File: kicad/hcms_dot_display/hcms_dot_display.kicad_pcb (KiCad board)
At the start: 2 copper layers, 35.6 x 42.1 mm, 36 parts, among them J1 Conn_01x13, J2 USB_C_Receptacle_USB2.0, J3 Conn_01x13, J4 Conn_01x10_Female, J5 Conn_01x10_Male, Q1 Q_PMOS_DSG, Q2 Q_PMOS_DSG, Q3 Q_PMOS_DSG, Q4 Q_PMOS_DSG, Q5 Q_PMOS_DSG, U1 ATtiny824-SSF, U2 FT231XS

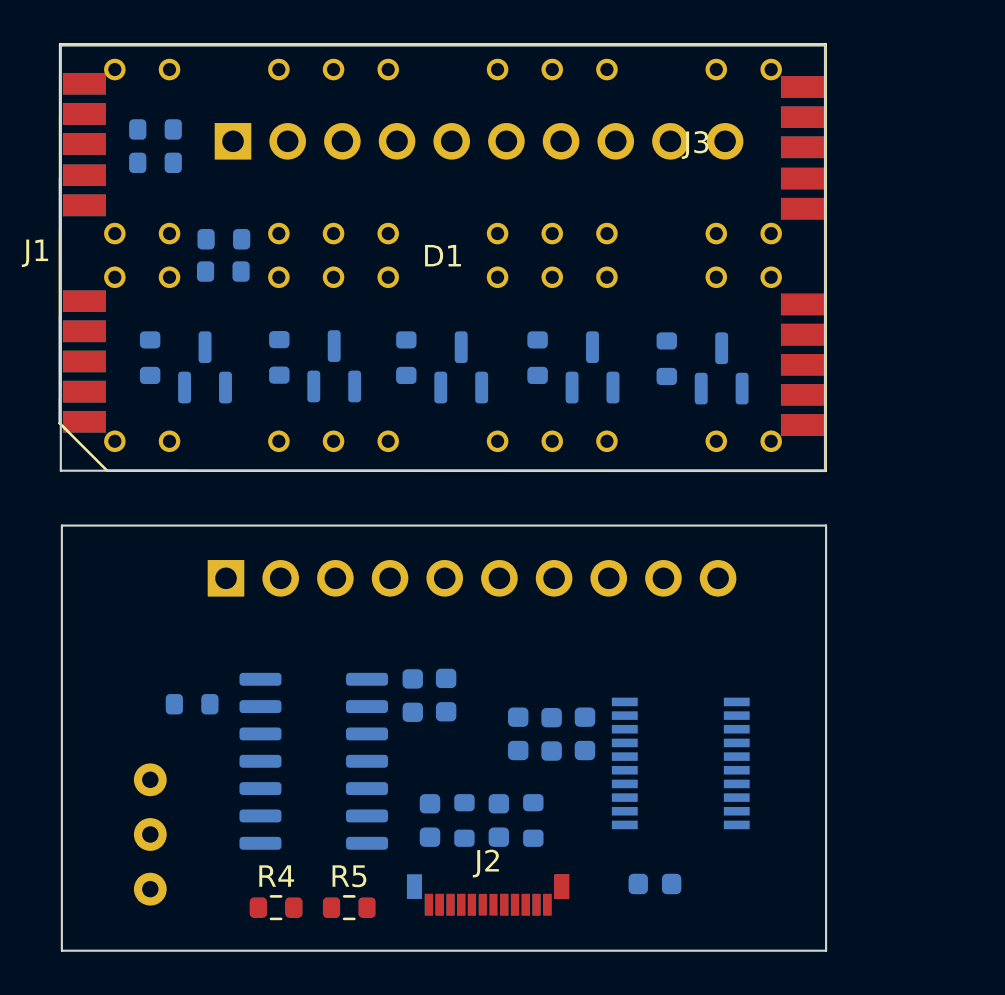
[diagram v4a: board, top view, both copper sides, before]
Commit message: fixed pot footprint, updated layout from schematics, changed board to board conn sch sym from 13 pin to 11 pin, reorgd sch sym to reflect stacked board design, added decoupling caps to top board
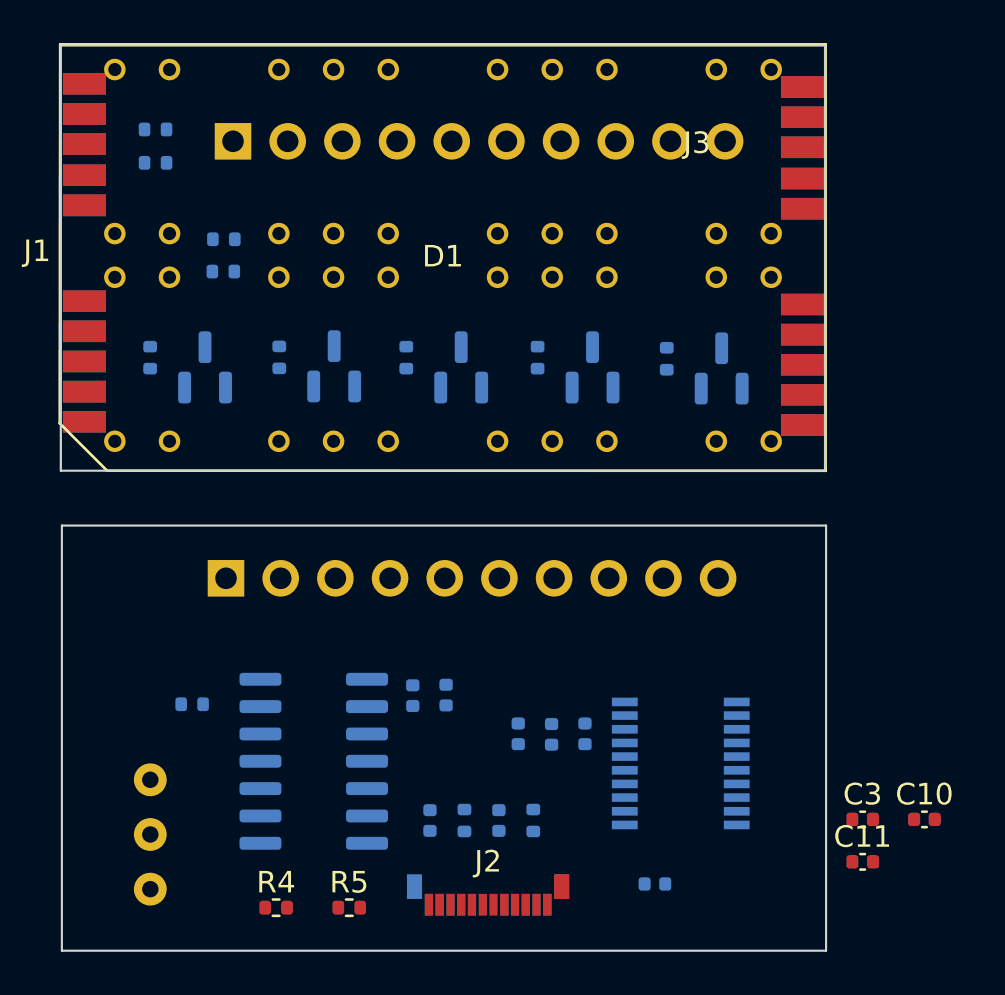
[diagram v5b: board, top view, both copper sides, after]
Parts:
- added C10: 10nF, Capacitor_SMD:C_0402_1005Metric, F.Cu at (174.9, 132.2)
- added C11: 10nF, Capacitor_SMD:C_0402_1005Metric, F.Cu at (172.0, 134.2)
- added C3: 100nF, Capacitor_SMD:C_0402_1005Metric, F.Cu at (172.0, 132.2)
- C1, C2, C4, C5, C6, C7, C8, C9: footprint Capacitor_SMD:C_0603_1608Metric -> Capacitor_SMD:C_0402_1005Metric
- R1, R10, R11, R12, R13, R14, R15, R2, R4, R5, R6, R7, R8, R9: footprint Resistor_SMD:R_0603_1608Metric -> Resistor_SMD:R_0402_1005Metric
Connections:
- J1 pad 10: /B_DATA -> /DAISY_B_DATA
- J1 pad 9: /A_DATA -> /DAISY_A_DATA
- J4 pad 1: /nBLNK -> +5V
- J4 pad 2: /MCU_DATA -> /MCU_COL_1
- J4 pad 3: /CLK -> /MCU_COL_2
- J4 pad 4: /MCU_COL_5 -> /MCU_COL_3
- J4 pad 6: /MCU_COL_3 -> /MCU_COL_5
- J4 pad 7: /MCU_COL_2 -> /nBLNK
- J4 pad 8: /MCU_COL_1 -> /CLK
- J4 pad 9: +5V -> /MCU_DATA
- J5 pad 1: /nBLNK -> +5V
- J5 pad 2: /MCU_DATA -> /MCU_COL_1
- J5 pad 3: /CLK -> /MCU_COL_2
- J5 pad 4: /MCU_COL_5 -> /MCU_COL_3
- J5 pad 6: /MCU_COL_3 -> /MCU_COL_5
- J5 pad 7: /MCU_COL_2 -> /nBLNK
- J5 pad 8: /MCU_COL_1 -> /CLK
- J5 pad 9: +5V -> /MCU_DATA

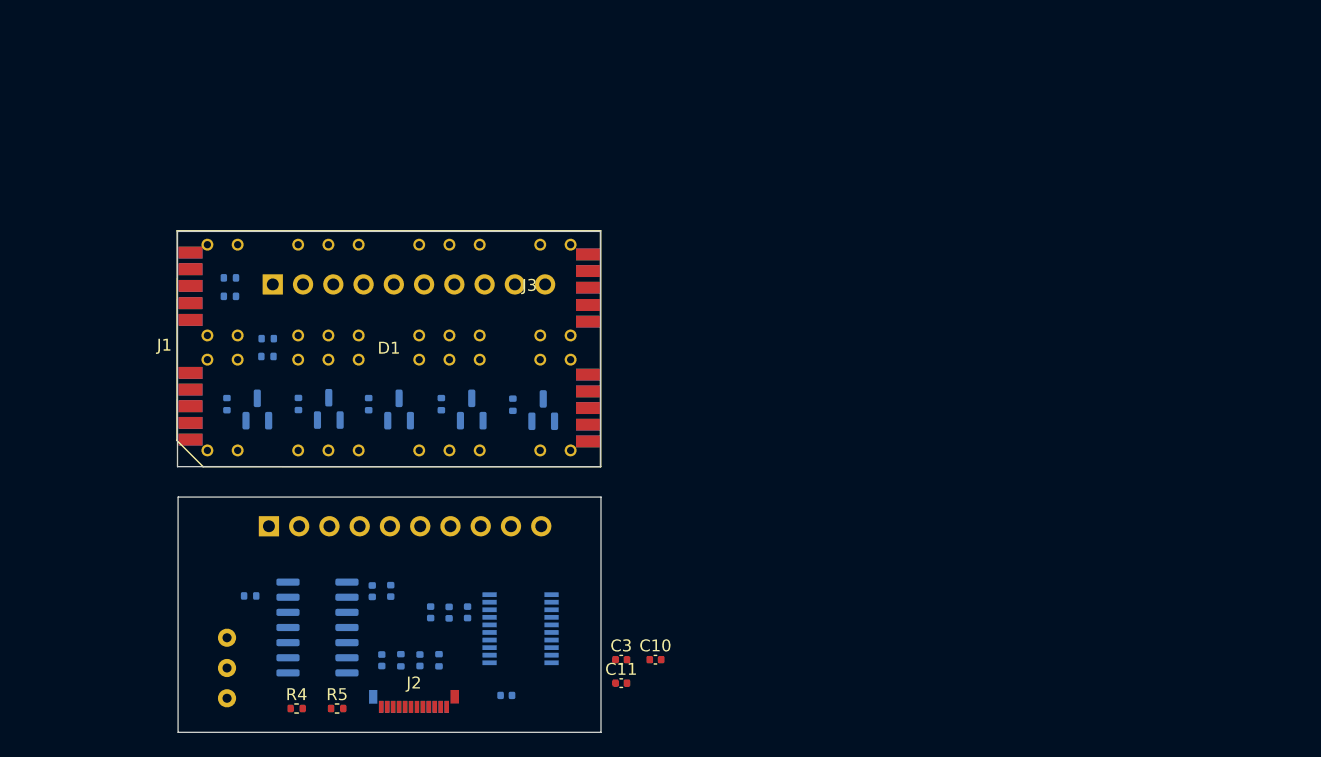
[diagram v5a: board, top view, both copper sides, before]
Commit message: fixed some footprints and edited placement
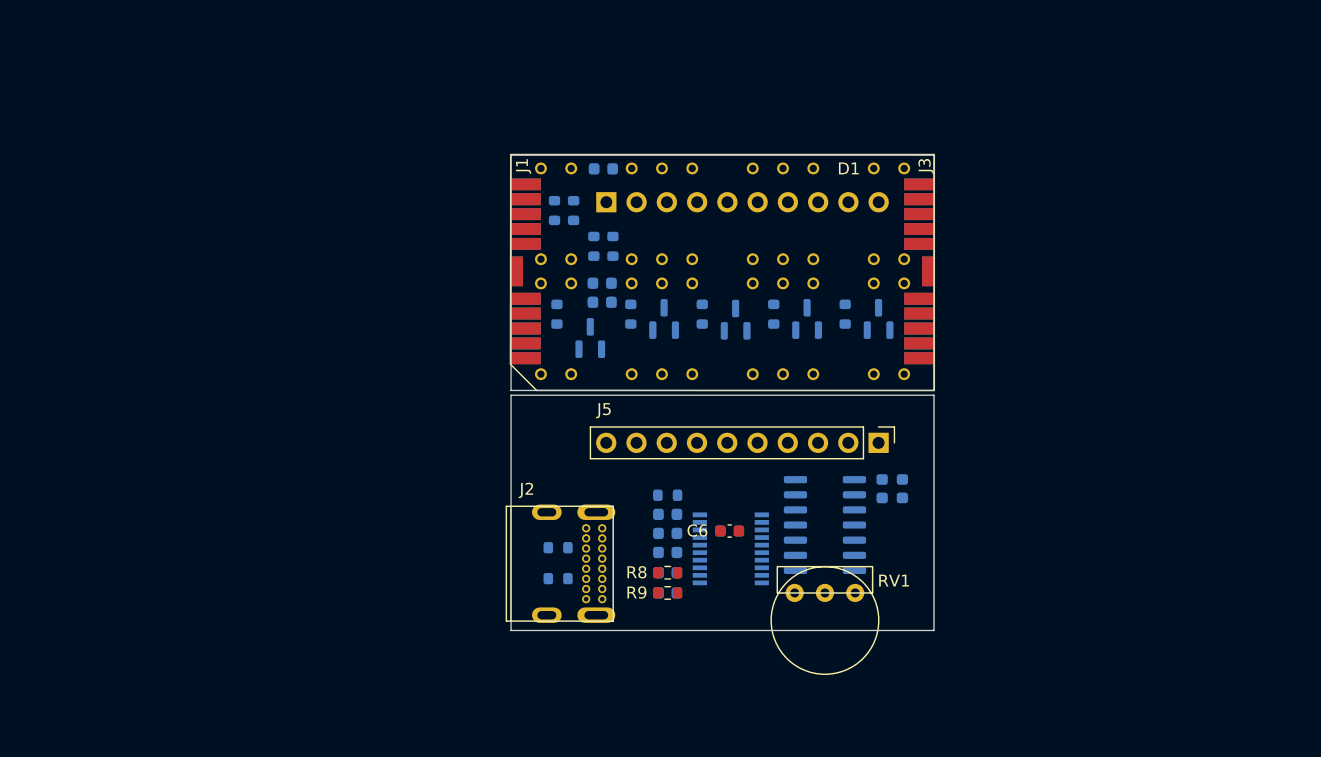
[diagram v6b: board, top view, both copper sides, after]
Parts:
- C1, C2, C4, C5, C7, C8, C9: footprint Capacitor_SMD:C_0402_1005Metric -> Capacitor_SMD:C_0603_1608Metric
- C10, C11, C3: footprint Capacitor_SMD:C_0402_1005Metric -> Capacitor_SMD:C_0603_1608Metric; moved to B.Cu
- C6: footprint Capacitor_SMD:C_0402_1005Metric -> Capacitor_SMD:C_0603_1608Metric; moved to F.Cu
- J1: value Conn_01x13 -> Conn_01x11; footprint hcms:board to board con -> hcms:input board to board con
- J2: footprint Connector_USB:USB_C_Plug_Molex_105444 -> hcms:213716-0001
- J3: value Conn_01x13 -> Conn_01x11; footprint hcms:board to board con -> hcms:output board to board con
- J5, RV1: moved to F.Cu
- R1, R10, R11, R12, R13, R14, R15, R2, R6, R7: footprint Resistor_SMD:R_0402_1005Metric -> Resistor_SMD:R_0603_1608Metric
- R4, R5: value R -> 10k; footprint Resistor_SMD:R_0402_1005Metric -> Resistor_SMD:R_0603_1608Metric; moved to B.Cu
- R8, R9: value R -> 27; footprint Resistor_SMD:R_0402_1005Metric -> Resistor_SMD:R_0603_1608Metric; moved to F.Cu
- moved J5 51.7 mm to (193.6, 114.0)
- moved RV1 50.6 mm to (189.1, 126.6), turned to 180 degrees
- moved C2 43.8 mm to (195.6, 117.8)
- moved C1 43.7 mm to (193.9, 117.8)
- moved U1 43.5 mm to (189.1, 120.9)
- moved C10 41.4 mm to (170.5, 91.0), turned to 180 degrees
- moved R15 36.1 mm to (175.9, 118.4)
- moved C11 33.6 mm to (170.4, 100.6), turned to 180 degrees
- moved C3 30.0 mm to (170.4, 102.2), turned to 180 degrees
- moved R1 30.0 mm to (171.3, 97.5), turned to 90 degrees
- moved R6 29.7 mm to (168.0, 94.5), turned to -90 degrees
- moved Q1 29.2 mm to (181.6, 103.7)
- moved Q5 29.2 mm to (193.6, 103.6)
- moved Q3 29.2 mm to (187.6, 103.6)
- moved Q4 29.1 mm to (175.6, 103.6)
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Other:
- board size 35.6 x 42.1 mm -> 35.5 x 39.9 mm
- board text added: "ap nl 0422"
- board text added: "dot display"
- board text added: "rev 1"

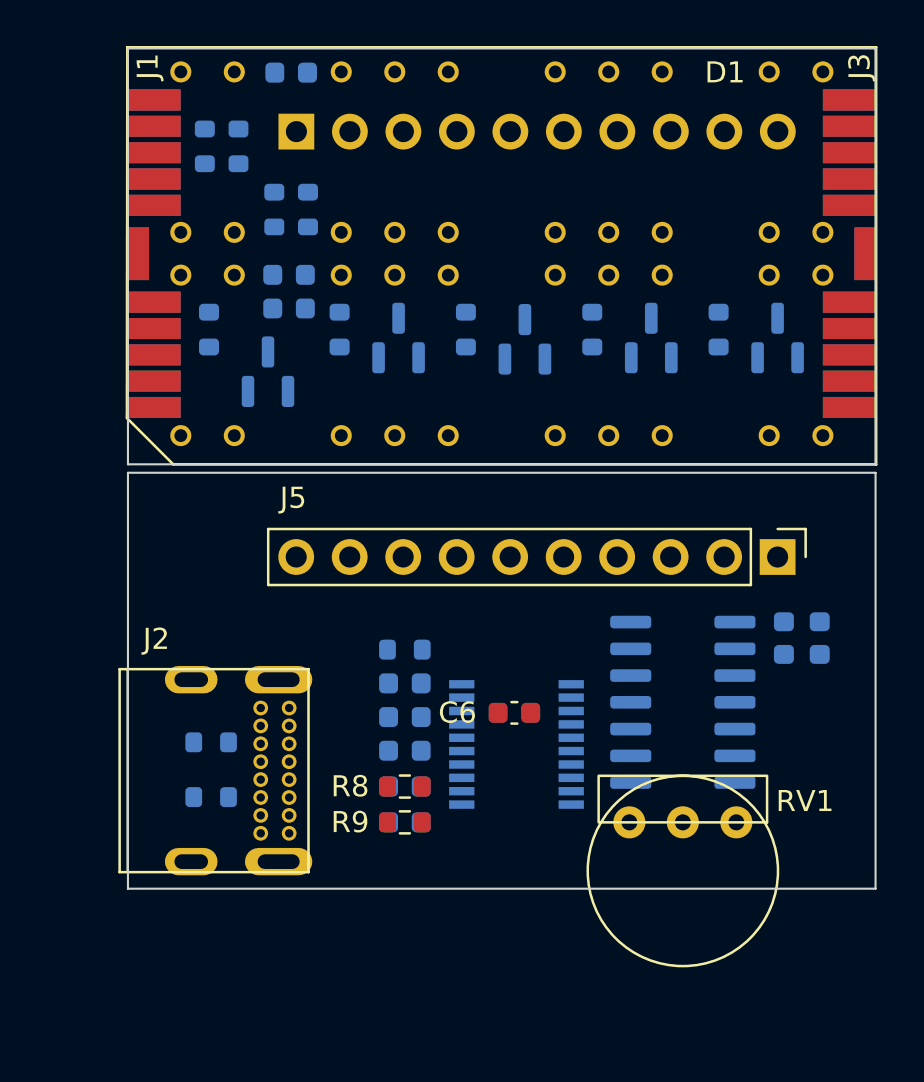
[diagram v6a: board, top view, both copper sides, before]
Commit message: 3d model environment variables lol
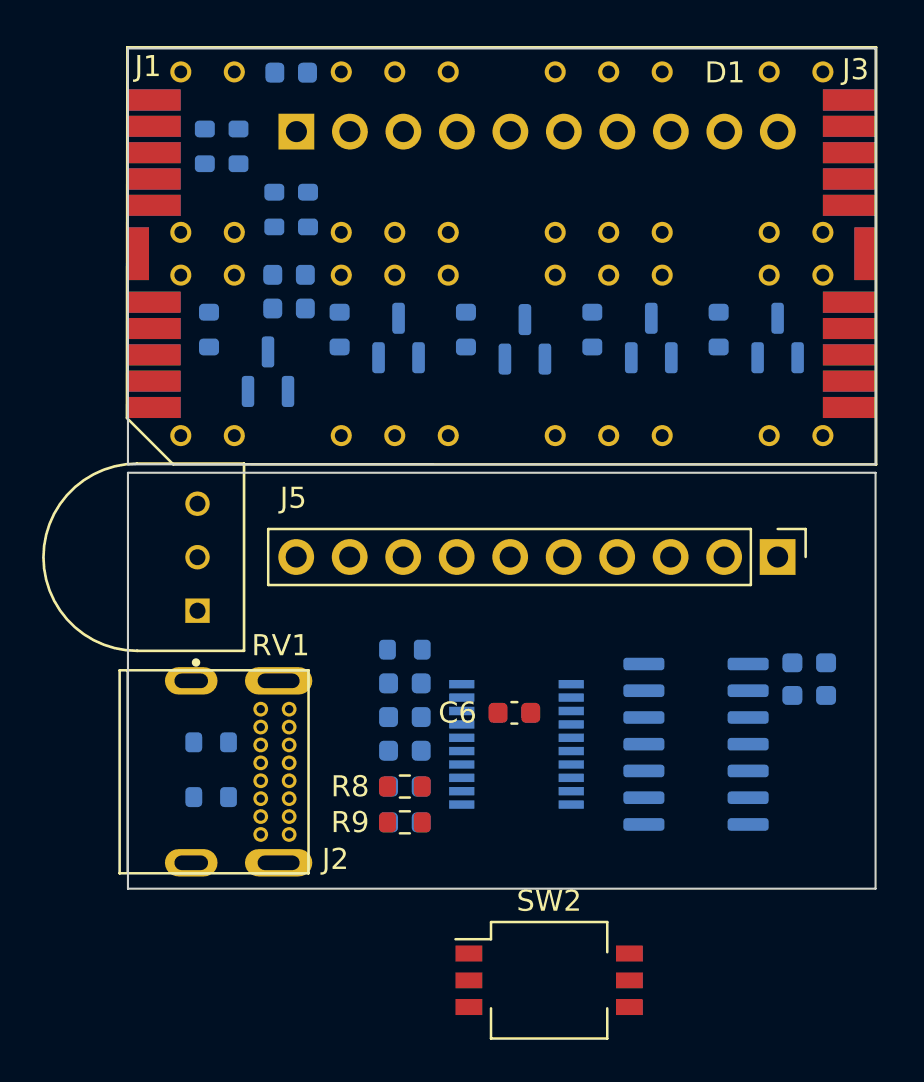
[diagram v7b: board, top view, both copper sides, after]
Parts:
- added SW2: SW_SPST, Button_Switch_SMD:SW_DIP_SPSTx03_Slide_KingTek_DSHP03TS_W7.62mm_P1.27mm, F.Cu at (182.8, 134.1)
- RV1: footprint hcms:3352T-1-503LF -> hcms:TRIM_3352T-1-201LF
- moved RV1 28.8 mm to (163.2, 114.0), turned to 90 degrees
- moved U1 2.09 mm to (189.7, 122.9)
- moved C1 1.99 mm to (194.3, 119.8)
- moved C2 1.97 mm to (195.9, 119.8)
- moved J2 0.06 mm to (166.8, 124.2)
